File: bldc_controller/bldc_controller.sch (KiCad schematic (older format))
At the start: 30 parts

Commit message: christmas work
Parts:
- removed C?: 68u, symbol Device:C
- removed C? (x3): C_Small, symbol Device:C_Small
- removed J?: Vbat, symbol Connector_Generic:Conn_01x02
- removed J?: V, symbol Connector_Generic:Conn_01x02
- removed J?: Conn_01x03, symbol Connector_Generic:Conn_01x03
- removed L?: 340u, symbol Device:L
- removed Q? (x2): Q_NMOS_GSD, symbol Device:Q_NMOS_GSD
- removed TP? (x2): TestPoint, symbol Connector:TestPoint
- added C? (x4): C, symbol Device:C
- added C? (x2): 12p, symbol Device:C
- added C?: 4u7, symbol Device:C_Small
- added C? (x13): 100n, symbol Device:C_Small
- added C? (x2): 2u2, symbol Device:C_Small
- added C? (x3): C_Small, symbol Device:C_Small
- added C? (x2): 10n, symbol Device:C
- added D?: D, symbol Device:D
- added D?: D_Schottky, symbol Device:D_Schottky
- added D?: BLUE, symbol Device:LED
- added F?: Polyfuse, symbol Device:Polyfuse
- added FB?: Ferrite_Bead, symbol Device:Ferrite_Bead
- added J?: Screw_Terminal_01x02, symbol Connector:Screw_Terminal_01x02
- added J?: Screw_Terminal_01x03, symbol Connector:Screw_Terminal_01x03
- added J?: USB_B_Micro, symbol Connector:USB_B_Micro
- added J?: SWD, symbol Connector_Generic:Conn_02x05_Odd_Even
- added L?: L, symbol Device:L
- added L?: 39n, symbol Device:L
- added Q?: Q_PMOS_GSD, symbol Device:Q_PMOS_GSD
- added R?: 47, symbol Device:R
- added R? (x4): R, symbol Device:R
- added R?: 10k, symbol Device:R
- added R?: 1k5, symbol Device:R
- added SW?: SW_SPDT, symbol Switch:SW_SPDT
- added U?: TPS54360DDA, Package_SO:TI_SO-PowerPAD-8_ThermalVias, symbol Regulator_Switching:TPS54360DDA
- added U?: STM32F407ZETx, Package_QFP:LQFP-144_20x20mm_P0.5mm, symbol MCU_ST_STM32F4:STM32F407ZETx
- added U?: USBLC6-2SC6, Package_TO_SOT_SMD:SOT-23-6, symbol Power_Protection:USBLC6-2SC6
- added Y?: 16MHz, symbol Device:Crystal_GND24
- IC? (x3): symbol SamacSys_Parts:IRS2003PBF -> bldc_controller-rescue:IRS2003PBF-SamacSys_Parts
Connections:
- net labels added: +3.3V, +3.3VA, +48V, +5V, BOOT0, BUCK_BOOT, BUCK_EN, BUCK_FB, BUCK_IN, BUCK_SW, DRIVE_A, DRIVE_B, DRIVE_C, GATE_AH, GATE_AL, GATE_BH, GATE_BL, GATE_CH, GATE_CL, HSE_IN, HSE_OUT, LED_STATUS, LO_A, LO_B, LO_C, NRST, SWCLK, SWDIO, SWO, USB_CONN_D+, USB_CONN_D-, USB_D+, USB_D-, VOUT_A, VOUT_B, VOUT_C
- net labels removed: DrA, DrB, DrC, Ha, Hb, Hc, La, Lb, Lc, Va, Vb, Vbat, Vc, Vinv
- wire segments 95 -> 176
- no-connect marks 0 -> 108
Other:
- note removed: "3-phase Inverter"
- note removed: "Buck SMPS"
- note removed: "MOSFET drivers"

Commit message: add current sensors
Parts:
- removed C? (x3): C, symbol Device:C
- removed D?: D, symbol Device:D
- removed D?: D_Schottky, symbol Device:D_Schottky
- removed L?: L, symbol Device:L
- removed Q?: Q_PMOS_GSD, symbol Device:Q_PMOS_GSD
- removed R? (x4): R, symbol Device:R
- removed U?: TPS54360DDA, Package_SO:TI_SO-PowerPAD-8_ThermalVias, symbol Regulator_Switching:TPS54360DDA
- added C?: 2.2u, symbol bldc_controller-rescue:C-Device
- added C? (x4): 0.1u, symbol bldc_controller-rescue:C-Device
- added C?: C-Device, symbol bldc_controller-rescue:C-Device
- added IC? (x3): ACS37002LMABTR-066B3, SOIC127P1030X265-16N, symbol ACS37002LMABTR-066B3:ACS37002LMABTR-066B3
- added IC?: LF33CV, TO255P460X1020X2008-3P, symbol LF33CV:LF33CV
- added PS?: R-78HB3.3-0.5L, R78HB3305L, symbol R-78HB3.3-0.5L:R-78HB3.3-0.5L
- added Q?: Q_PMOS_GSD-Device, symbol bldc_controller-rescue:Q_PMOS_GSD-Device
- C? (x4): symbol Device:C -> bldc_controller-rescue:C-Device
- C? (x19): symbol Device:C_Small -> bldc_controller-rescue:C_Small-Device
- C?: value C -> 10u; symbol Device:C -> bldc_controller-rescue:C-Device
- D? (x3): symbol Device:D_Small -> bldc_controller-rescue:D_Small-Device
- D?: symbol Device:LED -> bldc_controller-rescue:LED-Device
- F?: symbol Device:Polyfuse -> bldc_controller-rescue:Polyfuse-Device
- FB?: symbol Device:Ferrite_Bead -> bldc_controller-rescue:Ferrite_Bead-Device
- J?: symbol Connector:Screw_Terminal_01x02 -> bldc_controller-rescue:Screw_Terminal_01x02-Connector
- J?: symbol Connector:Screw_Terminal_01x03 -> bldc_controller-rescue:Screw_Terminal_01x03-Connector
- J?: symbol Connector:USB_B_Micro -> bldc_controller-rescue:USB_B_Micro-Connector
- J?: symbol Connector_Generic:Conn_02x05_Odd_Even -> bldc_controller-rescue:Conn_02x05_Odd_Even-Connector_Generic
- L?: symbol Device:L -> bldc_controller-rescue:L-Device
- Q? (x6): symbol Device:Q_NMOS_GSD -> bldc_controller-rescue:Q_NMOS_GSD-Device
- R? (x6): symbol Device:R_Small -> bldc_controller-rescue:R_Small-Device
- R? (x3): symbol Device:R -> bldc_controller-rescue:R-Device
- SW?: symbol Switch:SW_SPDT -> bldc_controller-rescue:SW_SPDT-Switch
- U?: symbol MCU_ST_STM32F4:STM32F407ZETx -> bldc_controller-rescue:STM32F407ZETx-MCU_ST_STM32F4
- U?: symbol Power_Protection:USBLC6-2SC6 -> bldc_controller-rescue:USBLC6-2SC6-Power_Protection
- Y?: symbol Device:Crystal_GND24 -> bldc_controller-rescue:Crystal_GND24-Device
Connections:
- net labels added: #A_CURR_OCF, #B_CURR_OCF, #C_CURR_OCF, A_CURR_VOC, A_CURR_VOUT, A_CURR_VREF, B_CURR_VOC, B_CURR_VOUT, B_CURR_VREF, C_CURR_VOC, C_CURR_VOUT, C_CURR_VREF, GAIN_SEL_0, MOT_A, MOT_B, MOT_C
- net labels removed: BUCK_BOOT, BUCK_EN, BUCK_FB, BUCK_SW
- wire segments 176 -> 272
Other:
- moved on the sheet: IC?

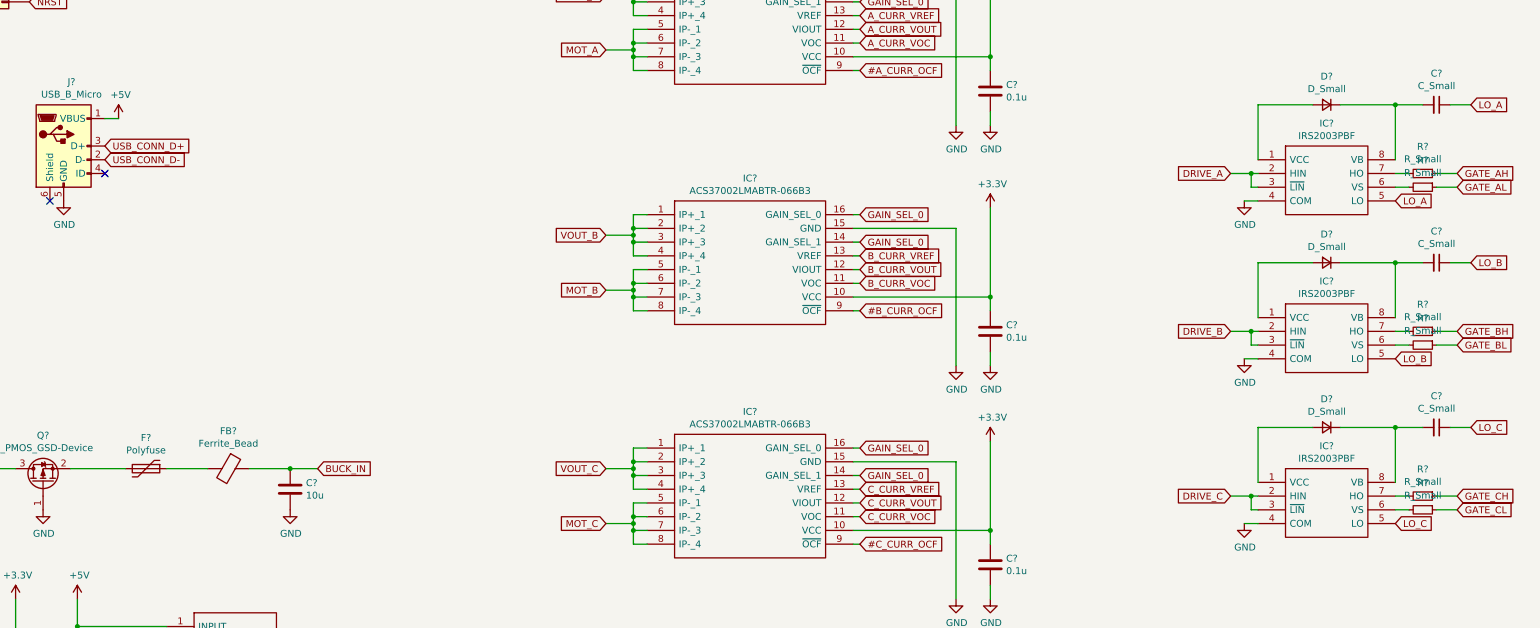
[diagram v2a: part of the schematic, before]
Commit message: partially fixed drivers
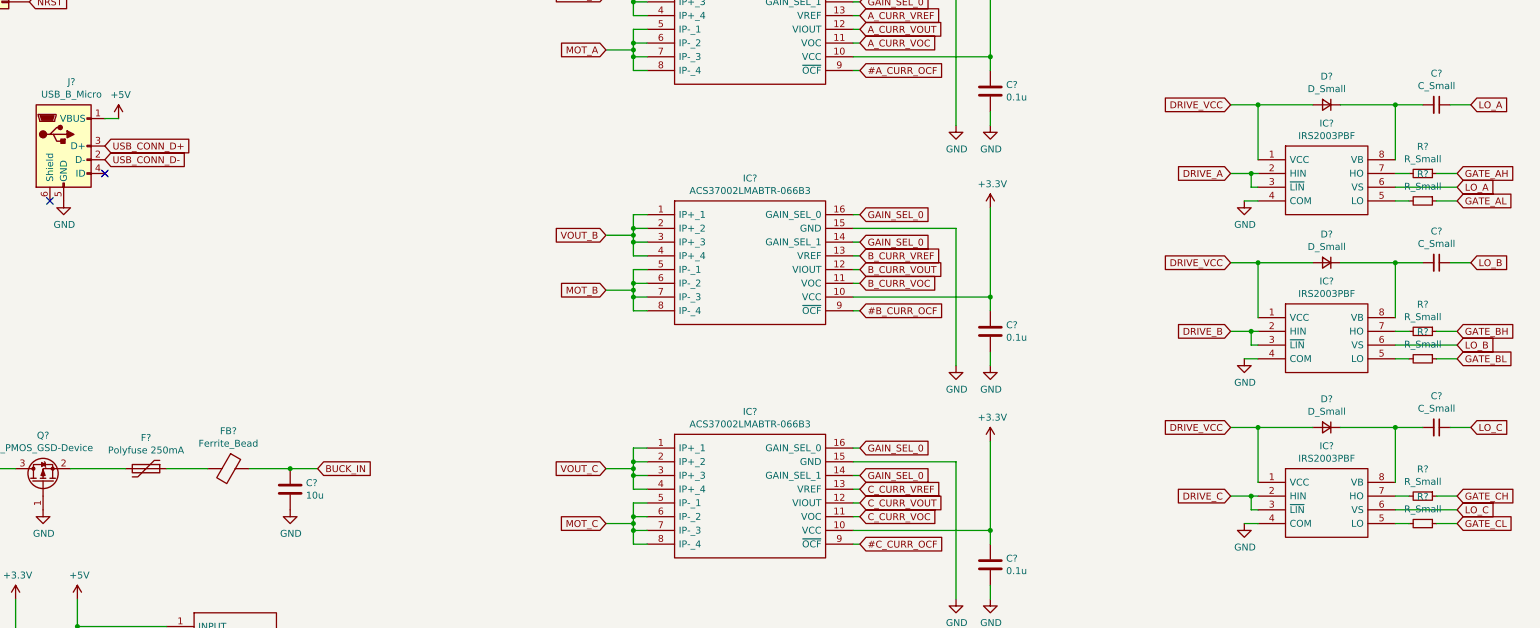
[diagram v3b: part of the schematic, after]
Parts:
- F?: value Polyfuse -> Polyfuse 250mA
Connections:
- net LO_A: now also IC?.6 (VS); no longer IC?.5 (LO)
- net LO_B: now also IC?.6 (VS); no longer IC?.5 (LO)
- net LO_C: now also IC?.6 (VS); no longer IC?.5 (LO)
- net DRIVE_VCC: now reaches D?.2 (A), IC?.1 (VCC)
- net DRIVE_VCC: now also D?.2 (A), D?.2 (A), IC?.1 (VCC), IC?.1 (VCC)
- net at R?.2: now also IC?.5 (LO); no longer IC?.6 (VS) (x3)
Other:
- moved on the sheet: R?
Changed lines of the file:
@@
 L bldc_controller-rescue:R_Small-Device R?
 U 1 1 617D7765
-P 18500 9050
-F 0 "R?" V 18304 9050 50  0000 C CNN
-F 1 "R_Small" V 18395 9050 50  0000 C CNN
-F 2 "" H 18500 9050 50  0001 C CNN
-F 3 "~" H 18500 9050 50  0001 C CNN
-	1    18500 9050
+P 18500 9150
+F 0 "R?" V 18304 9150 50  0000 C CNN
+F 1 "R_Small" V 18395 9150 50  0000 C CNN
+F 2 "" H 18500 9150 50  0001 C CNN
+F 3 "~" H 18500 9150 50  0001 C CNN
+	1    18500 9150
 	0    1    1    0
 $EndComp
@@
 	18400 8950 18300 8950
 Wire Wire Line
-	18300 9050 18400 9050
+	18300 9150 18400 9150
 Wire Wire Line
 	18600 8950 18750 8950
 Wire Wire Line
-	18600 9050 18750 9050
+	18600 9150 18750 9150
 Wire Wire Line
 	17200 9150 17300 9150
@@
 $EndComp
 Wire Wire Line
-	17700 9600 17300 9600
-Wire Wire Line
 	17300 9600 17300 10000
 $Comp
@@
 L bldc_controller-rescue:R_Small-Device R?
 U 1 1 617F0EDD
-P 18500 10200
-F 0 "R?" V 18304 10200 50  0000 C CNN
-F 1 "R_Small" V 18395 10200 50  0000 C CNN
-F 2 "" H 18500 10200 50  0001 C CNN
-F 3 "~" H 18500 10200 50  0001 C CNN
-	1    18500 10200
+P 18500 10300
+F 0 "R?" V 18304 10300 50  0000 C CNN
+F 1 "R_Small" V 18395 10300 50  0000 C CNN
+F 2 "" H 18500 10300 50  0001 C CNN
+F 3 "~" H 18500 10300 50  0001 C CNN
+	1    18500 10300
 	0    1    1    0
 $EndComp
@@
 	18400 10100 18300 10100
 Wire Wire Line
-	18300 10200 18400 10200
+	18300 10300 18400 10300
 Wire Wire Line
 	18600 10100 18750 10100
 Wire Wire Line
-	18600 10200 18750 10200
+	18600 10300 18750 10300
 Wire Wire Line
 	17200 10300 17300 10300
@@
 Wire Wire Line
 	18300 9600 18300 10000
-$Comp
-L bldc_controller-rescue:IRS2003PBF-SamacSys_Parts IC?
-U 1 1 61804574
-P 17300 11200
-F 0 "IC?" H 17800 11465 50  0000 C CNN
-F 1 "IRS2003PBF" H 17800 11374 50  0000 C CNN
-F 2 "DIP762W56P254L988H533Q8N" H 18150 11300 50  0001 L CNN
-F 3 "http://uk.rs-online.com/web/p/products/0496000" H 18150 11200 50  0001 L CNN
-F 4 "Infineon IRS2003PBF Dual Half Bridge MOSFET Power Driver, 0.6A 8-Pin, PDIP" H 18150 11100 50  0001 L CNN "Description"
-F 5 "5.33" H 18150 11000 50  0001 L CNN "Height"
-F 6 "0496000" H 18150 10900 50  0001 L CNN "RS Part Number"
-F 7 "http://uk.rs-online.com/web/p/products/0496000" H 18150 10800 50  0001 L CNN "RS Price/Stock"
-F 8 "Infineon" H 18150 10700 50  0001 L CNN "Manufacturer_Name"
-F 9 "IRS2003PBF" H 18150 10600 50  0001 L CNN "Manufacturer_Part_Number"
-F 10 "70017392" H 18150 10500 50  0001 L CNN "Allied_Number"
-	1    17300 11200
-	1    0    0    -1
-$EndComp
 $Comp
 L bldc_controller-rescue:GND-power #PWR?
@@
 $EndComp
 Wire Wire Line
-	17700 10800 17300 10800
-Wire Wire Line
 	17300 10800 17300 11200
 $Comp
@@
 L bldc_controller-rescue:R_Small-Device R?
 U 1 1 6180459B
-P 18500 11400
-F 0 "R?" V 18304 11400 50  0000 C CNN
-F 1 "R_Small" V 18395 11400 50  0000 C CNN
-F 2 "" H 18500 11400 50  0001 C CNN
-F 3 "~" H 18500 11400 50  0001 C CNN
-	1    18500 11400
+P 18500 11500
+F 0 "R?" V 18304 11500 50  0000 C CNN
+F 1 "R_Small" V 18395 11500 50  0000 C CNN
+F 2 "" H 18500 11500 50  0001 C CNN
+F 3 "~" H 18500 11500 50  0001 C CNN
+	1    18500 11500
 	0    1    1    0
 $EndComp
@@
 	18400 11300 18300 11300
 Wire Wire Line
-	18300 11400 18400 11400
-Wire Wire Line
-	18600 11300 18750 11300
-Wire Wire Line
-	18600 11400 18750 11400
+	18300 11500 18400 11500
+Wire Wire Line
+	18600 11500 18750 11500
 Wire Wire Line
 	17200 11500 17300 11500
@@
 Text GLabel 18750 8950 2    50   Input ~ 0
 GATE_AH
-Text GLabel 18750 9050 2    50   Input ~ 0
+Text GLabel 18750 9150 2    50   Input ~ 0
 GATE_AL
 Text GLabel 14000 4000 0    50   Input ~ 0
@@
 Text GLabel 18750 10100 2    50   Input ~ 0
 GATE_BH
-Text GLabel 18750 10200 2    50   Input ~ 0
+Text GLabel 18750 10300 2    50   Input ~ 0
 GATE_BL
 Text GLabel 18750 11300 2    50   Input ~ 0
 GATE_CH
-Text GLabel 18750 11400 2    50   Input ~ 0
+Text GLabel 18750 11500 2    50   Input ~ 0
 GATE_CL
 Text GLabel 15450 4000 0    50   Input ~ 0
@@
 	18500 8450 18300 8450
 Connection ~ 18300 8450
-Text GLabel 18300 9150 2    50   Input ~ 0
+Text GLabel 18750 9050 2    50   Input ~ 0
 LO_A
 $Comp
@@
 Wire Wire Line
 	18500 10800 18300 10800
-Text GLabel 18300 10300 2    50   Input ~ 0
+Text GLabel 18750 10200 2    50   Input ~ 0
 LO_B
-Text GLabel 18300 11500 2    50   Input ~ 0
-LO_C
 Connection ~ 18300 9600
 Connection ~ 18300 10800
@@
 P 9200 11100
 F 0 "F?" V 8975 11100 50  0000 C CNN
-F 1 "Polyfuse" V 9066 11100 50  0000 C CNN
+F 1 "Polyfuse 250mA" V 9066 11100 50  0000 C CNN
 F 2 "" H 9250 10900 50  0001 L CNN
 F 3 "~" H 9200 11100 50  0001 C CNN
@@
 Wire Wire Line
 	9100 14050 8900 14050
+Wire Wire Line
+	18300 9050 18750 9050
+Wire Wire Line
+	18300 10200 18750 10200
+Wire Wire Line
+	18600 11300 18750 11300
+Text GLabel 18750 11400 2    50   Input ~ 0
+LO_C
+$Comp
+L bldc_controller-rescue:IRS2003PBF-SamacSys_Parts IC?
+U 1 1 61804574
+P 17300 11200
+F 0 "IC?" H 17800 11465 50  0000 C CNN
+F 1 "IRS2003PBF" H 17800 11374 50  0000 C CNN
+F 2 "DIP762W56P254L988H533Q8N" H 18150 11300 50  0001 L CNN
+F 3 "http://uk.rs-online.com/web/p/products/0496000" H 18150 11200 50  0001 L CNN
+F 4 "Infineon IRS2003PBF Dual Half Bridge MOSFET Power Driver, 0.6A 8-Pin, PDIP" H 18150 11100 50  0001 L CNN "Description"
+F 5 "5.33" H 18150 11000 50  0001 L CNN "Height"
+F 6 "0496000" H 18150 10900 50  0001 L CNN "RS Part Number"
+F 7 "http://uk.rs-online.com/web/p/products/0496000" H 18150 10800 50  0001 L CNN "RS Price/Stock"
+F 8 "Infineon" H 18150 10700 50  0001 L CNN "Manufacturer_Name"
+F 9 "IRS2003PBF" H 18150 10600 50  0001 L CNN "Manufacturer_Part_Number"
+F 10 "70017392" H 18150 10500 50  0001 L CNN "Allied_Number"
+	1    17300 11200
+	1    0    0    -1
+$EndComp
+Wire Wire Line
+	18300 11400 18750 11400
+Text GLabel 17100 8450 0    50   Input ~ 0
+DRIVE_VCC
+Wire Wire Line
+	17100 8450 17300 8450
+Connection ~ 17300 8450
+Text GLabel 17100 9600 0    50   Input ~ 0
+DRIVE_VCC
+Text GLabel 17100 10800 0    50   Input ~ 0
+DRIVE_VCC
+Wire Wire Line
+	17100 9600 17300 9600
+Connection ~ 17300 9600
+Wire Wire Line
+	17300 9600 17700 9600
+Wire Wire Line
+	17100 10800 17300 10800
+Connection ~ 17300 10800
+Wire Wire Line
+	17300 10800 17700 10800
 $EndSCHEMATC

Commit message: add voltage sensing
added voltage sensing circuitry (voltage divider -> op-amp unity buffer) and organised schematic
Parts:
- added C?: 100n, symbol bldc_controller-rescue:C_Small-Device
- added C? (x4): 0.1u, symbol bldc_controller-rescue:C-Device
- added IC?: mcp6004-e_p, DIP781W56P254L1918H533Q14N, symbol mcp6004-e_p:mcp6004-e_p
- added R? (x4): 170k, symbol bldc_controller-rescue:R-Device
- added R? (x4): 10k, symbol bldc_controller-rescue:R-Device
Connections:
- net +3V3: now also C?.1, IC?.4 (VDD)
- net +48V: now also R?.1
- net GND: now also C?.1, C?.1, C?.1, C?.1, C?.2, R?.2, R?.2, R?.2, R?.2
- net MOT_A: now also R?.1
- net MOT_B: now also R?.1
- net MOT_C: now also R?.1
- new net BATT_BUFF: IC?.13 (VIND-), IC?.14 (VOUTD)
- new net BATT_SENSE: C?.2, IC?.12 (VIND+), R?.1, R?.2
- new net MOT_A_BUFF: IC?.1 (VOUTA), IC?.2 (VINA-)
- new net MOT_A_SENSE: C?.2, IC?.3 (VINA+), R?.1, R?.2
- new net MOT_B_BUFF: IC?.6 (VINB-), IC?.7 (VOUTB)
- new net MOT_B_SENSE: C?.2, IC?.5 (VINB+), R?.1, R?.2
- new net MOT_C_BUFF: IC?.8 (VOUTC), IC?.9 (VINC-)
- new net MOT_C_SENSE: C?.2, IC?.10 (VINC+), R?.1, R?.2
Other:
- note added: "Microcontroller"
- note added: "Note - 3-pin header for switching µC power source needs to go here"
- note added: "Note - these need to go to ADC pins"
- note added: "Power MOSFETs and MOSFET drivers"
- note added: "Protection and Regulation"
- note added: "Voltage and Current Sensing"
- moved on the sheet: C?, D?, F?, FB?, IC?, J?, L?, PS?, Q?, R?, SW?, U?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

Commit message: 3 pin connector and bootstrap values
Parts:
- added J?: Conn_01x03_Male, symbol Connector:Conn_01x03_Male
- C? (x3): value C_Small -> 100n
- IC?: symbol mcp6004-e_p:mcp6004-e_p -> bldc_controller-rescue:mcp6004-e_p-mcp6004-e_p
- IC? (x3): symbol ACS37002LMABTR-066B3:ACS37002LMABTR-066B3 -> bldc_controller-rescue:ACS37002LMABTR-066B3-ACS37002LMABTR-066B3
- IC?: symbol LF33CV:LF33CV -> bldc_controller-rescue:LF33CV-LF33CV
- PS?: symbol R-78HB3.3-0.5L:R-78HB3.3-0.5L -> bldc_controller-rescue:R-78HB3.3-0.5L-R-78HB3.3-0.5L
- R? (x6): value R_Small -> 4.7
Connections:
- net +3V3: now also J?.2 (Pin_2); no longer C?.1, IC?.3 (OUTPUT), PS?.3 (+VOUT)
- net LO_A: no longer IC?.6 (VS)
- net VOUT_A: now also IC?.6 (VS)
- new net 3V3_BAT: J?.1 (Pin_1), PS?.3 (+VOUT)
- new net 3V3_USB: C?.1, IC?.3 (OUTPUT), J?.3 (Pin_3)
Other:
- note removed: "Note - 3-pin header for switching µC power source needs to go here"
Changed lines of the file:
@@
 P 14500 3050
 F 0 "R?" V 14304 3050 50  0000 C CNN
-F 1 "R_Small" V 14395 3050 50  0000 C CNN
+F 1 "4.7" V 14395 3050 50  0000 C CNN
 F 2 "" H 14500 3050 50  0001 C CNN
 F 3 "~" H 14500 3050 50  0001 C CNN
@@
 P 14500 3250
 F 0 "R?" V 14304 3250 50  0000 C CNN
-F 1 "R_Small" V 14395 3250 50  0000 C CNN
+F 1 "4.7" V 14395 3250 50  0000 C CNN
 F 2 "" H 14500 3250 50  0001 C CNN
 F 3 "~" H 14500 3250 50  0001 C CNN
@@
 P 14500 4400
 F 0 "R?" V 14304 4400 50  0000 C CNN
-F 1 "R_Small" V 14395 4400 50  0000 C CNN
+F 1 "4.7" V 14395 4400 50  0000 C CNN
 F 2 "" H 14500 4400 50  0001 C CNN
 F 3 "~" H 14500 4400 50  0001 C CNN
@@
 P 14500 4600
 F 0 "R?" V 14304 4600 50  0000 C CNN
-F 1 "R_Small" V 14395 4600 50  0000 C CNN
+F 1 "4.7" V 14395 4600 50  0000 C CNN
 F 2 "" H 14500 4600 50  0001 C CNN
 F 3 "~" H 14500 4600 50  0001 C CNN
@@
 P 14500 5750
 F 0 "R?" V 14304 5750 50  0000 C CNN
-F 1 "R_Small" V 14395 5750 50  0000 C CNN
+F 1 "4.7" V 14395 5750 50  0000 C CNN
 F 2 "" H 14500 5750 50  0001 C CNN
 F 3 "~" H 14500 5750 50  0001 C CNN
@@
 P 14500 5950
 F 0 "R?" V 14304 5950 50  0000 C CNN
-F 1 "R_Small" V 14395 5950 50  0000 C CNN
+F 1 "4.7" V 14395 5950 50  0000 C CNN
 F 2 "" H 14500 5950 50  0001 C CNN
 F 3 "~" H 14500 5950 50  0001 C CNN
@@
 P 14600 2550
 F 0 "C?" V 14371 2550 50  0000 C CNN
-F 1 "C_Small" V 14462 2550 50  0000 C CNN
+F 1 "100n" V 14462 2550 50  0000 C CNN
 F 2 "" H 14600 2550 50  0001 C CNN
 F 3 "~" H 14600 2550 50  0001 C CNN
@@
 	14500 2550 14300 2550
 Connection ~ 14300 2550
-Text GLabel 14750 3150 2    50   Input ~ 0
-LO_A
 $Comp
 L bldc_controller-rescue:C_Small-Device C?
@@
 P 14600 3900
 F 0 "C?" V 14371 3900 50  0000 C CNN
-F 1 "C_Small" V 14462 3900 50  0000 C CNN
+F 1 "100n" V 14462 3900 50  0000 C CNN
 F 2 "" H 14600 3900 50  0001 C CNN
 F 3 "~" H 14600 3900 50  0001 C CNN
@@
 P 14600 5250
 F 0 "C?" V 14371 5250 50  0000 C CNN
-F 1 "C_Small" V 14462 5250 50  0000 C CNN
+F 1 "100n" V 14462 5250 50  0000 C CNN
 F 2 "" H 14600 5250 50  0001 C CNN
 F 3 "~" H 14600 5250 50  0001 C CNN
@@
 Connection ~ 4050 14050
 $Comp
-L R-78HB3.3-0.5L:R-78HB3.3-0.5L PS?
+L bldc_controller-rescue:R-78HB3.3-0.5L-R-78HB3.3-0.5L PS?
 U 1 1 61EC1EAE
 P 6500 13850
@@
 L bldc_controller-rescue:+3.3V-power #PWR?
 U 1 1 61F69FCC
-P 6350 13700
-F 0 "#PWR?" H 6350 13550 50  0001 C CNN
-F 1 "+3.3V" H 6365 13873 50  0000 C CNN
-F 2 "" H 6350 13700 50  0001 C CNN
-F 3 "" H 6350 13700 50  0001 C CNN
-	1    6350 13700
+P 5750 13150
+F 0 "#PWR?" H 5750 13000 50  0001 C CNN
+F 1 "+3.3V" H 5765 13323 50  0000 C CNN
+F 2 "" H 5750 13150 50  0001 C CNN
+F 3 "" H 5750 13150 50  0001 C CNN
+	1    5750 13150
 	1    0    0    -1
 $EndComp
@@
 	6350 14050 6500 14050
 $Comp
-L LF33CV:LF33CV IC?
+L bldc_controller-rescue:LF33CV-LF33CV IC?
 U 1 1 6203DB57
 P 9550 13800
@@
 Wire Wire Line
 	8900 13600 8900 13800
-$Comp
-L bldc_controller-rescue:+3.3V-power #PWR?
-U 1 1 620611B1
-P 8450 13600
-F 0 "#PWR?" H 8450 13450 50  0001 C CNN
-F 1 "+3.3V" H 8465 13773 50  0000 C CNN
-F 2 "" H 8450 13600 50  0001 C CNN
-F 3 "" H 8450 13600 50  0001 C CNN
-	1    8450 13600
-	1    0    0    -1
-$EndComp
 Wire Wire Line
 	8450 13600 8450 14000
@@
 $EndComp
 $Comp
-L ACS37002LMABTR-066B3:ACS37002LMABTR-066B3 IC?
+L bldc_controller-rescue:ACS37002LMABTR-066B3-ACS37002LMABTR-066B3 IC?
 U 1 1 61FCEA3F
 P 13500 9350
@@
 $EndComp
 $Comp
-L ACS37002LMABTR-066B3:ACS37002LMABTR-066B3 IC?
+L bldc_controller-rescue:ACS37002LMABTR-066B3-ACS37002LMABTR-066B3 IC?
 U 1 1 62604CFA
 P 13500 11400
@@
 $EndComp
 $Comp
-L ACS37002LMABTR-066B3:ACS37002LMABTR-066B3 IC?
+L bldc_controller-rescue:ACS37002LMABTR-066B3-ACS37002LMABTR-066B3 IC?
 U 1 1 6263EDA6
 P 13500 13450
@@
 $EndComp
 $Comp
-L mcp6004-e_p:mcp6004-e_p IC?
+L bldc_controller-rescue:mcp6004-e_p-mcp6004-e_p IC?
 U 1 1 61FCADF0
 P 19100 12450
@@
 Text Notes 9800 8050 2    50   Italic 10
 Note - these need to go to ADC pins
-Text Notes 9050 13000 2    50   Italic 10
-Note - 3-pin header for switching µC power source needs to go here
+$Comp
+L Connector:Conn_01x03_Male J?
+U 1 1 61FEECD1
+P 5000 13150
+F 0 "J?" H 4700 13450 50  0000 C CNN
+F 1 "Conn_01x03_Male" H 4750 13350 50  0000 C CNN
+F 2 "" H 5000 13150 50  0001 C CNN
+F 3 "~" H 5000 13150 50  0001 C CNN
+	1    5000 13150
+	1    0    0    -1
+$EndComp
+Text GLabel 8450 13600 0    50   Input ~ 0
+3V3_USB
+Text GLabel 14750 3150 2    50   Input ~ 0
+VOUT_A
+Text GLabel 5200 13250 2    50   Input ~ 0
+3V3_USB
+Text GLabel 6350 13700 0    50   Input ~ 0
+3V3_BAT
+Wire Wire Line
+	5200 13150 5750 13150
+Text GLabel 5200 13050 2    50   Input ~ 0
+3V3_BAT
 $EndSCHEMATC
